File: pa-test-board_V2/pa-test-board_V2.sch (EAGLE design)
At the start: 34 parts, among them J1 142-0701-851, J2 142-0701-851, J3 142-0701-851, J4 142-0701-851, SW1 TL36PO, U10 TQP9111

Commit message: Added 1st draft layout for Oliver
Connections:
- removed net N$25: C22.1, L4.2
- net N$1: now also C22.1, L4.2
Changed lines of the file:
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@@
 <?xml version="1.0" encoding="utf-8"?>
 <!DOCTYPE eagle SYSTEM "eagle.dtd">
-<eagle version="9.5.1">
+<eagle version="9.6.1">
 <drawing>
 <settings>
@@
 <setting verticaltext="up"/>
 </settings>
-<grid distance="0.05" unitdist="inch" unit="inch" style="lines" multiple="2" display="yes" altdistance="0.01" altunitdist="inch" altunit="inch"/>
+<grid distance="0.1" unitdist="inch" unit="inch" style="lines" multiple="1" display="no" altdistance="0.01" altunitdist="inch" altunit="inch"/>
 <layers>
 <layer number="1" name="Top" color="4" fill="1" visible="no" active="no"/>
@@
 </segment>
 </net>
-<net name="N$25" class="1">
-<segment>
-<pinref part="C22" gate="CE" pin="1"/>
-<wire x1="86.36" y1="119.38" x2="83.82" y2="119.38" width="0.1524" layer="91"/>
-<pinref part="L4" gate="L" pin="2"/>
-<wire x1="83.82" y1="119.38" x2="76.2" y2="119.38" width="0.1524" layer="91"/>
-<junction x="83.82" y="119.38"/>
-</segment>
-</net>
 <net name="N$27" class="1">
 <segment>
@@
 <segment>
 <pinref part="J2" gate="G$1" pin="RF"/>
-<wire x1="71.12" y1="119.38" x2="76.2" y2="119.38" width="0.1524" layer="91"/>
-</segment>
-</net>
+<pinref part="C22" gate="CE" pin="1"/>
+<wire x1="86.36" y1="119.38" x2="83.82" y2="119.38" width="0.1524" layer="91"/>
+<pinref part="L4" gate="L" pin="2"/>
+<wire x1="83.82" y1="119.38" x2="71.12" y2="119.38" width="0.1524" layer="91"/>
+<junction x="83.82" y="119.38"/>
+</segment>
+</net>

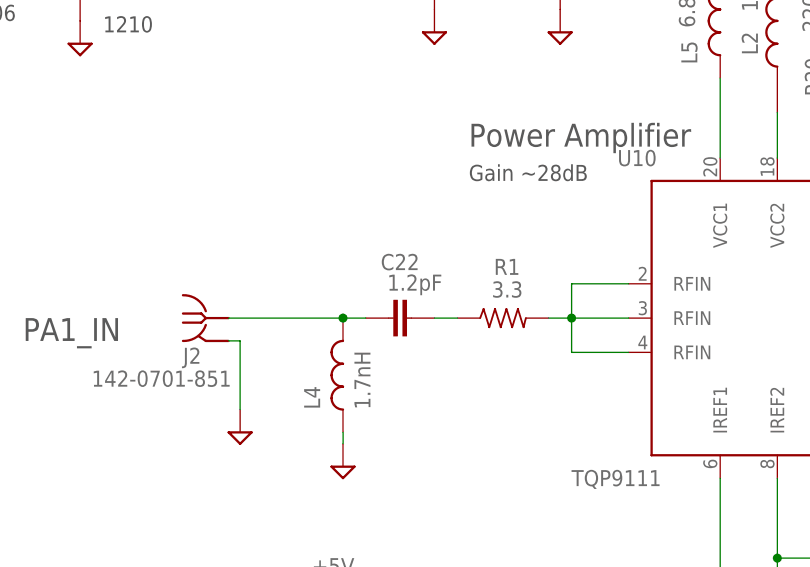
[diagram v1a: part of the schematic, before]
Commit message: Updated to tuned values, fixed BOM formatting.
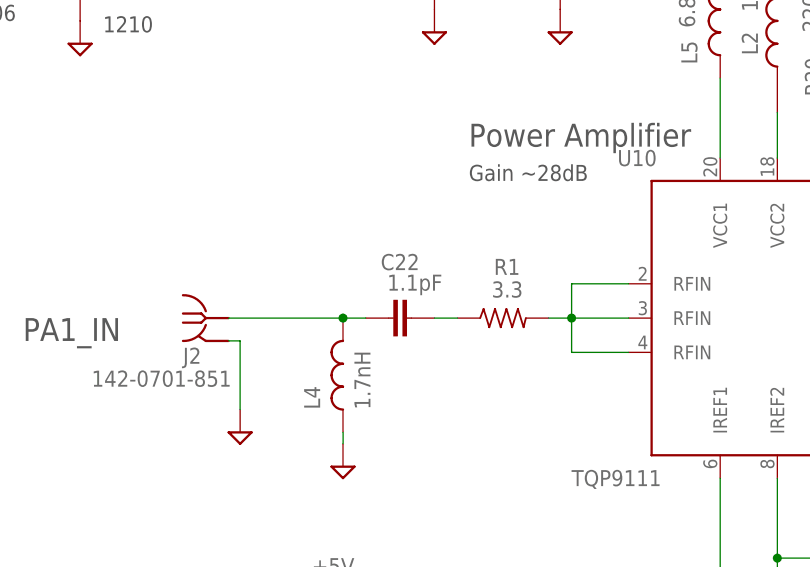
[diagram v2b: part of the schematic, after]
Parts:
- C22: value 1.2pF -> 1.1pF; DESCRIPTION Capacitor Thin Film 50V 1.2pF .02pFTol 0402 -> 50V 1.1pF .02pFTol ThinFilm 0402; MPN 04025J1R2PBSTR -> 04025J1R1PBSTR\500
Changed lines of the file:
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@@
 <attribute name="MPN" value="04025U3R0BAT2A"/>
 </part>
-<part name="C22" library="oresat-rcl" deviceset="C-EU" device="0402-C-NOSILK" value="1.2pF">
+<part name="C22" library="oresat-rcl" deviceset="C-EU" device="0402-C-NOSILK" value="1.1pF">
 <spice>
 <pinmapping spiceprefix="C">
@@
 </pinmapping>
 </spice>
-<attribute name="DESCRIPTION" value="Capacitor Thin Film 50V 1.2pF .02pFTol  0402"/>
+<attribute name="DESCRIPTION" value="50V 1.1pF .02pFTol ThinFilm 0402"/>
 <attribute name="MFR" value="AVX"/>
-<attribute name="MPN" value="04025J1R2PBSTR"/>
+<attribute name="MPN" value="04025J1R1PBSTR\500"/>
 </part>
 <part name="C23" library="oresat-rcl" deviceset="C-EU" device="0402-C-NOSILK" value="1.6pF">
